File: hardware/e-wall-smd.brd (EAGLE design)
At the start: 50.8 x 48.3 mm, 45 parts, among them IC1 74HCT595D, IC2 74HCT595D, IC3 74HCT595D, Q1 2N7002P, Q10 2N7002P, Q11 2N7002P, Q12 2N7002P, Q13 2N7002P, Q14 2N7002P, Q15 2N7002P, Q16 2N7002P, Q17 2N7002P, Q18 2N7002P, Q19 2N7002P, Q2 2N7002P, Q20 2N7002P, Q21 2N7002P, Q22 2N7002P, Q23 2N7002P, Q24 2N7002P, Q3 2N7002P, Q4 2N7002P, Q5 2N7002P, Q6 2N7002P, Q7 2N7002P, Q8 2N7002P, Q9 2N7002P, T1 BC547, T2 BC557, T3 BC547

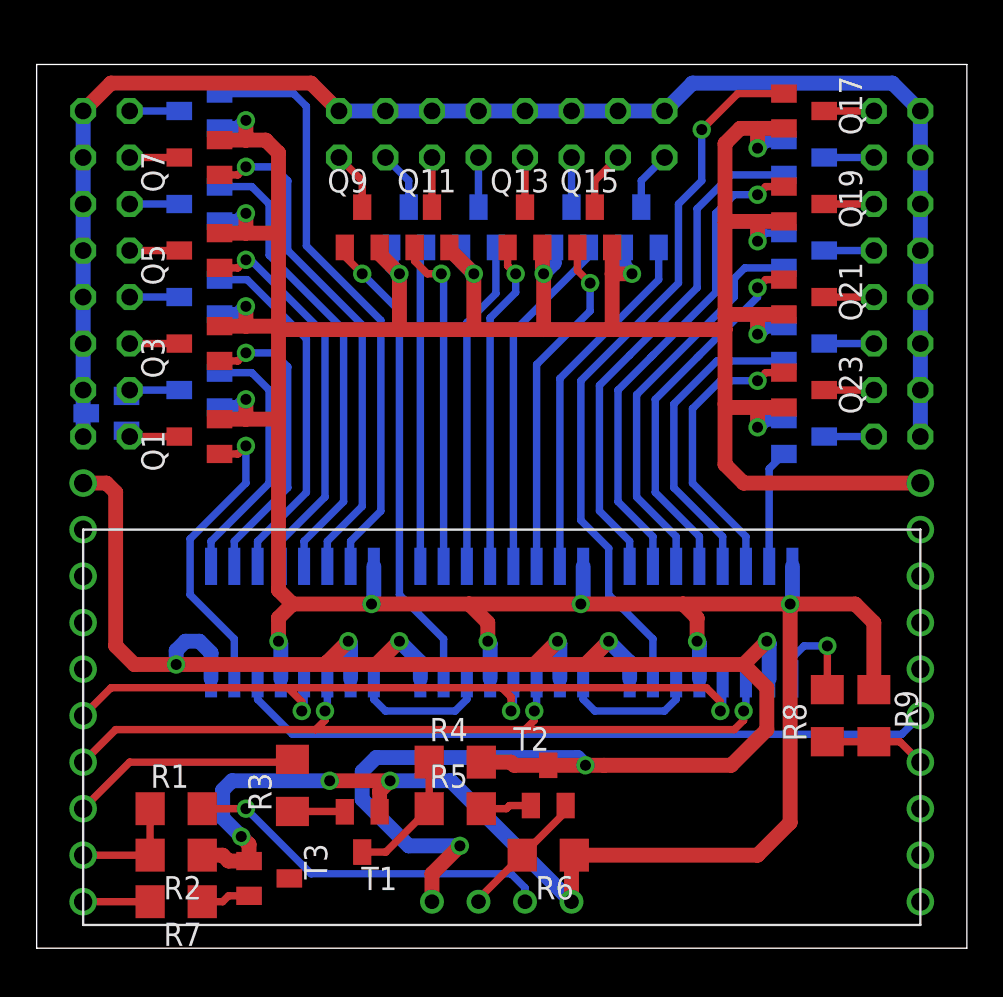
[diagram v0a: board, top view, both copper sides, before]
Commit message: Freilaufdiode ergänzt
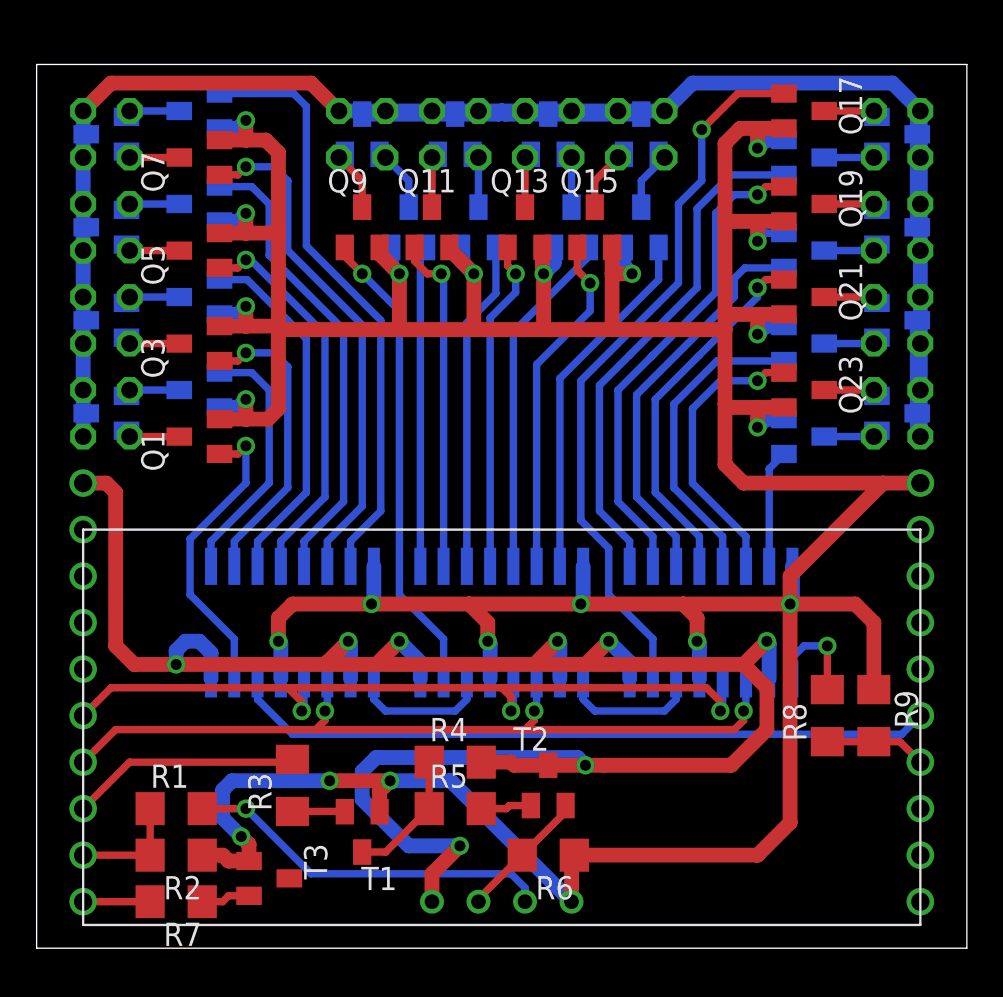
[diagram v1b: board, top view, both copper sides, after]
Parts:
- added D10, D11, D12, D2, D3, D4, D5, D6, D7, D8, D9: BAS40-05, diode:SOT23
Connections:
- net +12V: now also D10.3, D11.3, D12.3, D2.3, D3.3, D4.3, D5.3, D6.3, D7.3, D8.3, D9.3
- net OUT10: now also D6.2
- net OUT11: now also D6.1
- net OUT12: now also D7.2
- net OUT13: now also D7.1
- net OUT14: now also D8.2
- net OUT15: now also D8.1
- net OUT16: now also D9.2
- net OUT17: now also D9.1
- net OUT18: now also D10.2
- net OUT19: now also D10.1
- net OUT2: now also D2.2
- net OUT20: now also D11.2
- net OUT21: now also D11.1
- net OUT22: now also D12.2
- net OUT23: now also D12.1
- net OUT3: now also D2.1
- net OUT4: now also D3.2
- net OUT5: now also D3.1
- net OUT6: now also D4.2
- net OUT7: now also D4.1
- net OUT8: now also D5.2
- net OUT9: now also D5.1
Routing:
- net +12V: track 84.0 -> 112.8 mm
- net GND: track 266.7 -> 264.7 mm

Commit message: Schieberegister verschoben
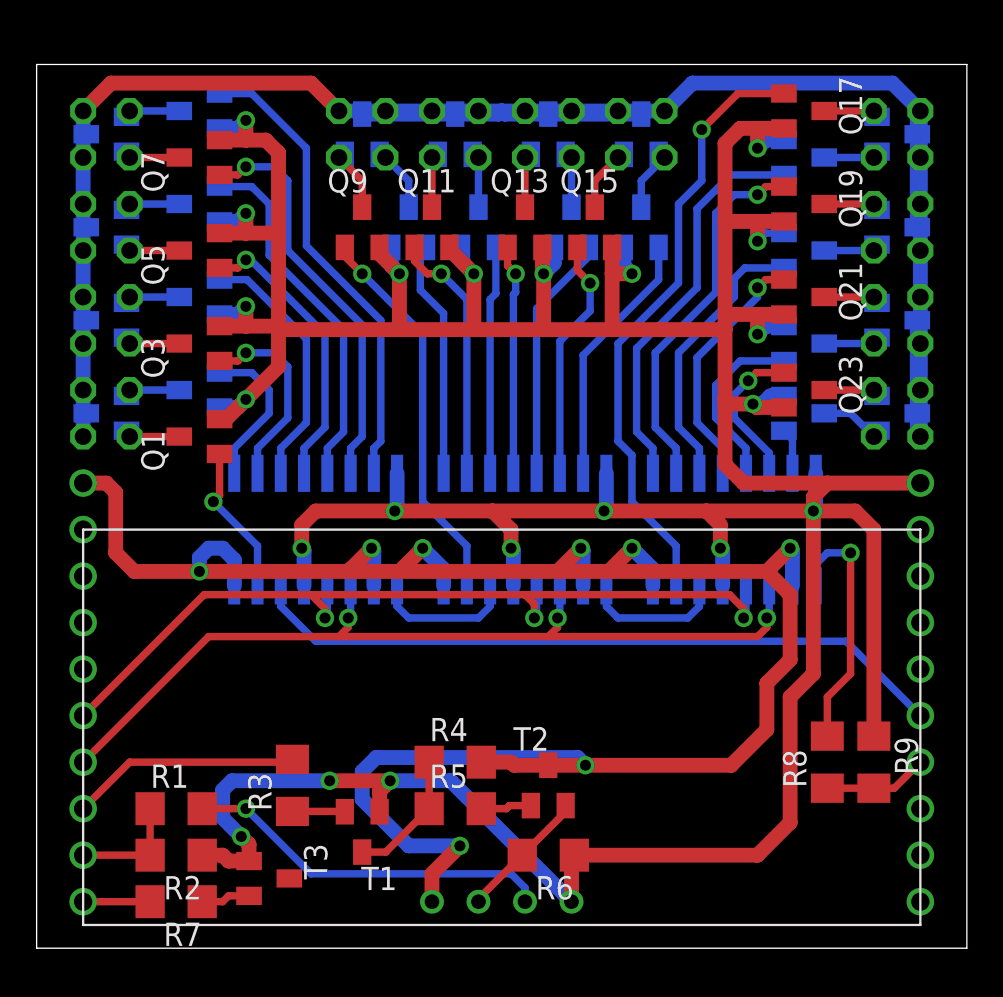
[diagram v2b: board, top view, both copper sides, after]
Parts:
- moved IC2 5.24 mm to (26.7, 22.9)
- moved IC3 5.24 mm to (38.1, 22.9)
- moved IC1 5.24 mm to (15.2, 22.9)
- moved R8 2.54 mm to (43.2, 10.2)
- moved R9 2.54 mm to (45.7, 10.2)
- moved Q24 1.27 mm to (41.9, 29.2)
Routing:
- net SIG0: track 16.6 -> 8.34 mm
- net SOMI: track 5.72 -> 13.9 mm
- net SIG22: track 15.6 -> 8.29 mm
- net SIG21: track 17.0 -> 9.76 mm
- net SIG7: track 32.5 -> 25.6 mm
- net SIG20: track 20.2 -> 13.7 mm
- net SIG19: track 21.8 -> 15.3 mm
- net SIG16: track 39.7 -> 33.4 mm
- net SIG18: track 26.6 -> 20.4 mm
- net SIG17: track 27.9 -> 21.7 mm
- net SIG3: track 19.6 -> 14.0 mm
- net SIG2: track 16.6 -> 11.0 mm
- net SIG13: track 19.1 -> 13.5 mm
- net SIG6: track 27.8 -> 22.1 mm
- net SIG5: track 25.5 -> 19.9 mm
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
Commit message: Leitungen für SPI umbenannt
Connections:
- net N$28 renamed SOMI_UC
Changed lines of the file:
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@@
 <wire x1="2.71" y1="44.45" x2="2.54" y2="44.45" width="0.8128" layer="16"/>
 </signal>
-<signal name="N$28">
+<signal name="SOMI_UC">
 <contactref element="R9" pad="2"/>
 <contactref element="R8" pad="1"/>
@@
 </signal>
 </signals>
-<errors>
-</errors>
 </board>
 </drawing>

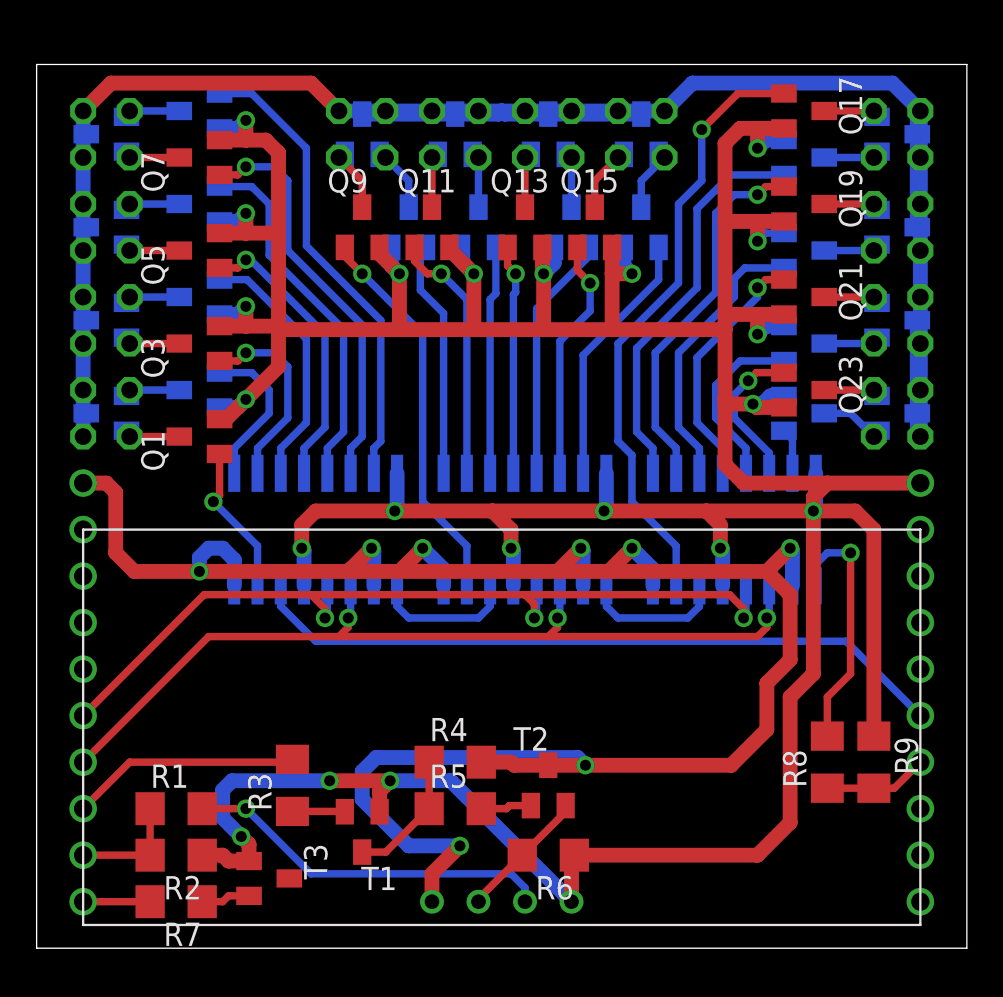
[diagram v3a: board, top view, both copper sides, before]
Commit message: Schieberegister verschoben
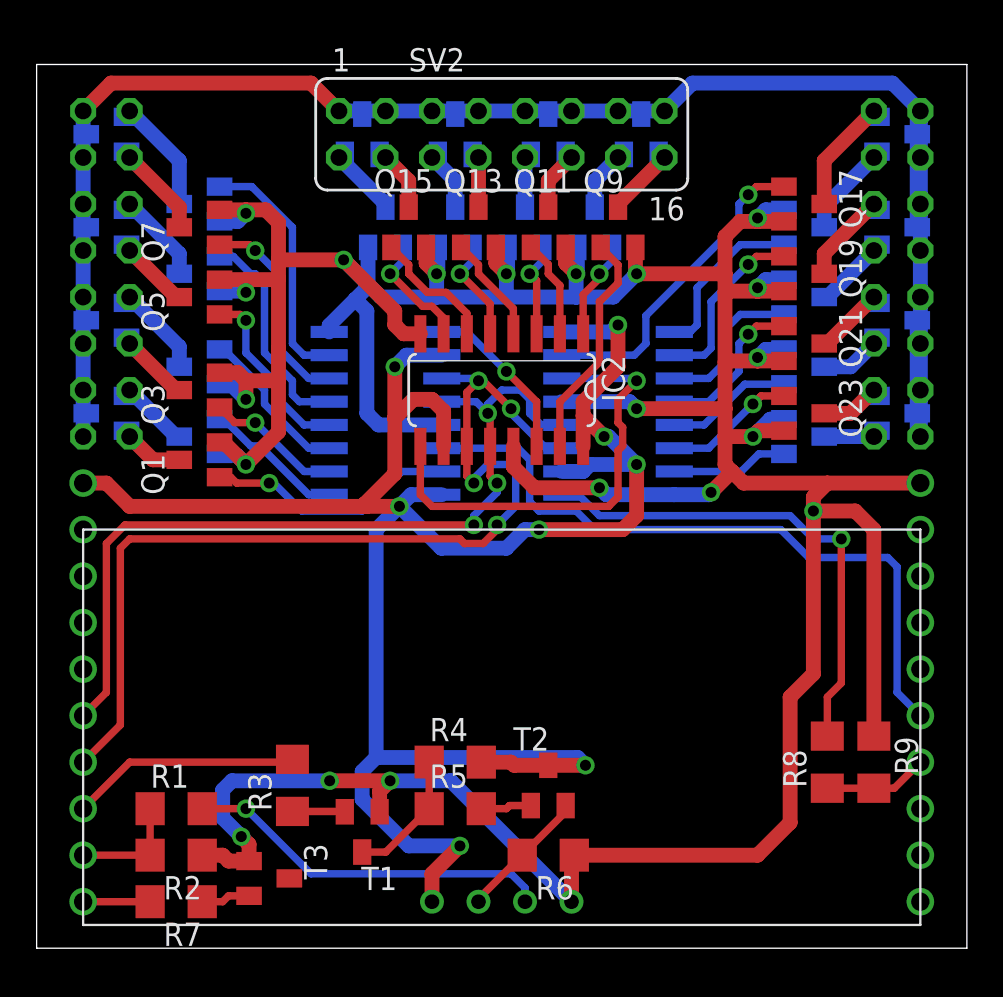
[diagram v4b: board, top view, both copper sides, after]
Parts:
- moved D5 15.2 mm to (33.0, 44.5)
- moved D8 15.2 mm to (17.8, 44.5)
- moved Q16 14.0 mm to (19.1, 39.4)
- moved Q9 14.0 mm to (31.8, 39.4)
- moved Q10 10.2 mm to (30.5, 39.4)
- moved Q15 10.2 mm to (20.3, 39.4)
- moved IC3 8.98 mm to (31.8, 29.2), turned to 270 degrees
- moved IC2 7.73 mm to (25.4, 30.5), flipped to the top
- moved IC1 7.41 mm to (19.1, 29.2), turned to 90 degrees
- moved Q11 6.35 mm to (27.9, 39.4)
- moved Q14 6.35 mm to (22.9, 39.4)
- moved D6 5.08 mm to (27.9, 44.5)
- moved D7 5.08 mm to (22.9, 44.5)
- moved Q17 5.08 mm to (41.9, 40.6)
- moved Q8 5.08 mm to (8.89, 40.6)
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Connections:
- net OUT10: now also D6.1; no longer D6.2
- net OUT11: now also D6.2; no longer D6.1
- net OUT12: now also D7.1; no longer D7.2
- net OUT13: now also D7.2; no longer D7.1
- net OUT14: now also D8.1; no longer D8.2
- net OUT15: now also D8.2; no longer D8.1
- net OUT8: now also D5.1; no longer D5.2
- net OUT9: now also D5.2; no longer D5.1
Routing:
- net GND: track 267.1 -> 246.4 mm, vias 21 -> 20
- net N$2: track 7.84 -> 25.0 mm, vias 0 -> 1
- net SIG16: track 33.4 -> 17.4 mm
- net +12V: track 112.8 -> 98.1 mm
- net SOMI: track 13.9 -> 27.4 mm
- net SIG17: track 21.7 -> 9.15 mm
- net SIG7: track 25.6 -> 13.5 mm
- net SIG18: track 20.4 -> 9.71 mm
- net SIG6: track 22.1 -> 11.6 mm
- net SIG8: track 21.2 -> 12.6 mm, vias 1 -> 0
- net SIG10: track 14.0 -> 5.38 mm, vias 1 -> 0
- net SIG5: track 19.9 -> 12.0 mm
- net SIG13: track 13.5 -> 5.69 mm, vias 0 -> 1
- net SIG9: track 13.0 -> 5.37 mm, vias 0 -> 1
- net SIG15: track 14.0 -> 6.51 mm, vias 0 -> 1
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
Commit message: Zusätzliches Schieberegister mit Treiber für mehr Strom
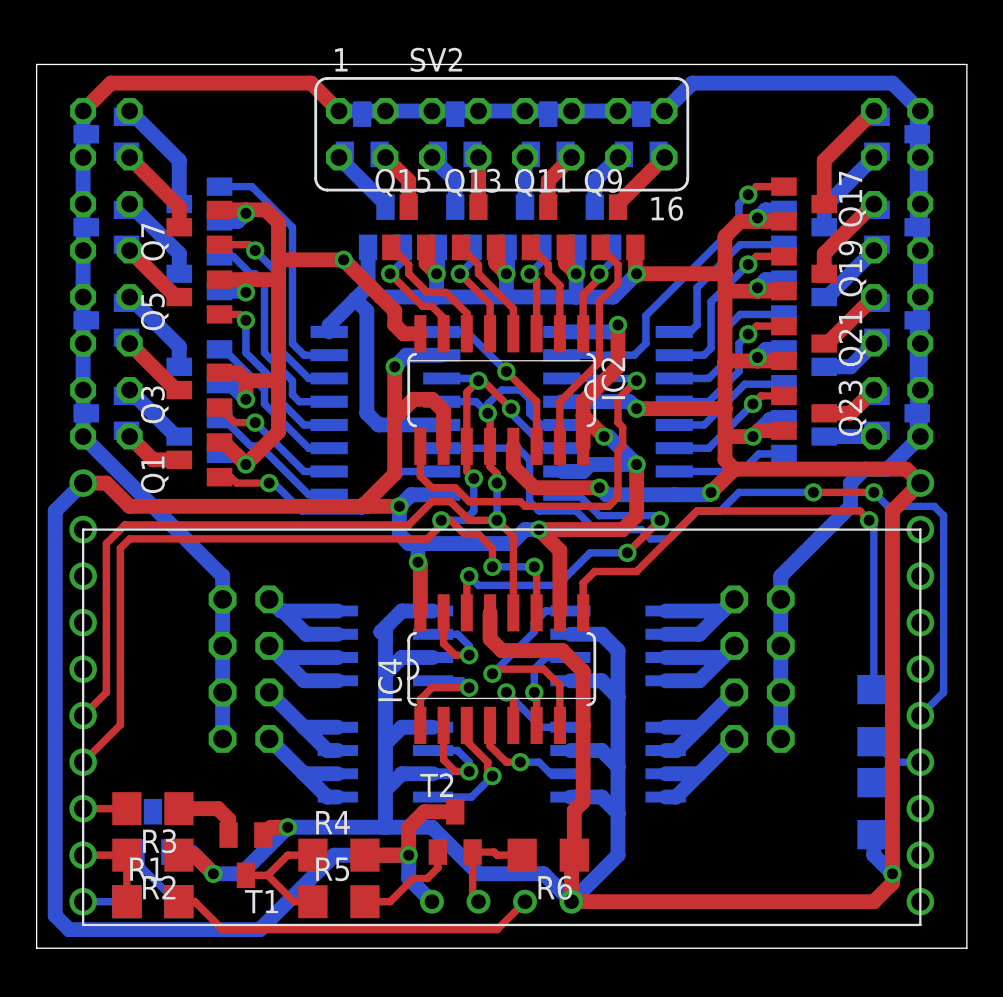
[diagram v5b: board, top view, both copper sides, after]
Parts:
- added IC4: 74HCT595D, 74xx-eu:SO16
- added Q25, Q26, Q27, Q28: IRF8313P, transistor-power:SO-08
- added SV4, SV5: (no value), con-lstb:MA04-2
- moved R4 8.13 mm to (16.5, 5.08)
- moved R5 8.13 mm to (16.5, 2.54)
- moved R3 7.73 mm to (6.35, 7.62), turned to 180 degrees
- moved T3 6.84 mm to (6.35, 6.35), flipped to the bottom, turned to 0 degrees
- moved T1 6.48 mm to (11.4, 5.08)
- moved T2 5.68 mm to (22.9, 6.35)
- moved R1 5.24 mm to (6.35, 2.54)
- moved R8 3.59 mm to (45.7, 12.7), flipped to the bottom
- moved R9 2.54 mm to (45.7, 7.62), flipped to the bottom, turned to 90 degrees
- moved R2 1.27 mm to (6.35, 5.08)
- moved R7 1.27 mm to (6.35, 2.54), flipped to the bottom, turned to 0 degrees
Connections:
- new net N$3: IC3.9, IC4.14
- new net OUT24: Q25.7, Q25.8, SV4.8
- new net OUT25: Q25.5, Q25.6, SV4.6
- new net OUT26: Q26.7, Q26.8, SV4.4
- new net OUT27: Q26.5, Q26.6, SV4.2
- new net OUT28: Q27.7, Q27.8, SV5.8
- new net OUT29: Q27.5, Q27.6, SV5.6
- new net OUT30: Q28.7, Q28.8, SV5.4
- new net OUT31: Q28.5, Q28.6, SV5.2
- new net SIG24: IC4.15, Q25.2
- new net SIG25: IC4.1, Q25.4
- new net SIG26: IC4.2, Q26.2
- new net SIG27: IC4.3, Q26.4
- new net SIG28: IC4.4, Q27.2
- new net SIG29: IC4.5, Q27.4
- new net SIG30: IC4.6, Q28.2
- new net SIG31: IC4.7, Q28.4
- net +12V: now also SV4.1, SV4.3, SV4.5, SV4.7, SV5.1, SV5.3, SV5.5, SV5.7
- net CLK: now also IC4.11
- net EN: now also IC4.12
- net GND: now also IC4.13, IC4.8, Q25.1, Q25.3, Q26.1, Q26.3, Q27.1, Q27.3, Q28.1, Q28.3
- net SOMI: now also IC4.9; no longer IC3.9
- net VCC: now also IC4.10, IC4.16
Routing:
- net GND: track 246.4 -> 307.1 mm, vias 20 -> 19
- net +12V: track 98.1 -> 138.2 mm
- net VCC: track 117.4 -> 138.1 mm
- net N$3: track 0.00 -> 20.1 mm, vias 0 -> 3
- net SIG31: track 0.00 -> 12.3 mm, vias 0 -> 1
- net TRIGGER_UC: track 12.5 -> 2.39 mm
- net OUT31: track 0.00 -> 8.55 mm
- net OUT30: track 0.00 -> 7.65 mm
- net OUT25: track 0.00 -> 7.65 mm
- net OUT24: track 0.00 -> 7.53 mm
- net SIG27: track 0.00 -> 7.06 mm, vias 0 -> 1
- net OUT26: track 0.00 -> 6.91 mm
- net OUT29: track 0.00 -> 6.91 mm
- net OUT27: track 0.00 -> 6.91 mm
- net OUT28: track 0.00 -> 6.91 mm
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
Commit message: Anschlüsse für Versorgung und Kupferflächen für MAsse und 12V
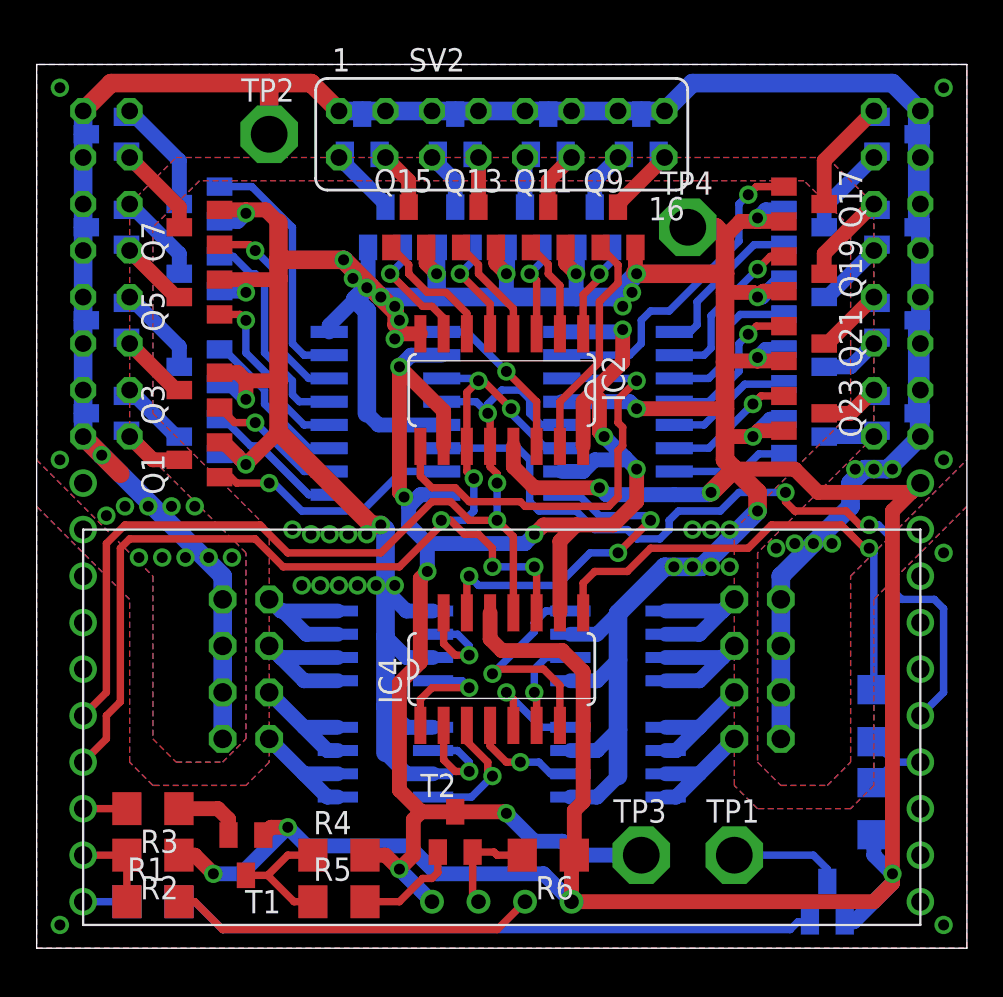
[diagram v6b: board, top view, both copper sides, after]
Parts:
- added TP1, TP2, TP3, TP4: PTR1PAD1-20, testpad:P1-20
- moved T3 37.0 mm to (43.2, 2.54)
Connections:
- removed net GND: IC1.13, IC1.8, IC2.13, IC2.8, IC3.13, IC3.8, IC4.13, IC4.8, Q1.2, Q10.2, Q11.2, Q12.2, Q13.2, Q14.2, Q15.2, Q16.2, Q17.2, Q18.2, Q19.2, Q2.2, Q20.2, Q21.2, Q22.2, Q23.2, Q24.2, Q25.1, Q25.3, Q26.1, Q26.3, Q27.1, Q27.3, Q28.1, Q28.3, Q3.2, Q4.2, Q5.2, Q6.2, Q7.2, Q8.2, Q9.2, R2.1, R6.1, R9.1, T1.E, T3.E, U$1.20, U$2.P$4
- new net +5V: IC1.10, IC1.16, IC2.10, IC2.16, IC3.10, IC3.16, IC4.10, IC4.16, R4.2, T2.E, TP3.TP, U$2.P$1
- new net CP: IC1.13, IC1.8, IC2.13, IC2.8, IC3.13, IC3.8, IC4.13, IC4.8, Q1.2, Q10.2, Q11.2, Q12.2, Q13.2, Q14.2, Q15.2, Q16.2, Q17.2, Q18.2, Q19.2, Q2.2, Q20.2, Q21.2, Q22.2, Q23.2, Q24.2, Q25.1, Q25.3, Q26.1, Q26.3, Q27.1, Q27.3, Q28.1, Q28.3, Q3.2, Q4.2, Q5.2, Q6.2, Q7.2, Q8.2, Q9.2, R2.1, R6.1, R9.1, T1.E, T3.E, TP4.TP, U$1.20, U$2.P$4
- net +12V: now also TP2.TP
- net POWER_ON: now also TP1.TP
- net VCC: no longer IC1.10, IC1.16, IC2.10, IC2.16, IC3.10, IC3.16, IC4.10, IC4.16, R4.2, T2.E, U$2.P$1
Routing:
- net CP: track 0.00 -> 327.9 mm, vias 0 -> 50
- net GND: track 307.1 -> 0.00 mm, vias 19 -> 0
- net VCC: track 138.1 -> 0.00 mm, vias 8 -> 0
- net +5V: track 0.00 -> 96.3 mm, vias 0 -> 9
- net N$36: track 3.78 -> 35.3 mm
- net POWER_ON: track 0.00 -> 6.07 mm
- net +12V: track 138.2 -> 143.8 mm, vias 0 -> 22
- net SOMI: track 28.4 -> 26.9 mm
- net EN: track 53.0 -> 54.2 mm
- net CLK: track 57.9 -> 59.2 mm
- net N$3: track 20.1 -> 19.1 mm
- net SIMO: track 43.8 -> 43.1 mm
- added copper zone on layer 1, net +12V
- added copper zone on layer 16, net +12V
- added copper zone on layer 1, net CP
- added copper zone on layer 16, net CP
